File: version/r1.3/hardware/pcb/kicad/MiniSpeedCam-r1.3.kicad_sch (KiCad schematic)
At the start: 101 parts, among them J1 Power terminal connector, J10 TF PUSH, J3 Open Vias, J4 Open Vias, J8 AFC01-S24FCC-00, Q1 L8050QLT1G, Q2 L8050QLT1G, SW1 TS36CA-0.7, SW3 TS-1088-AR02016, SW6 TS-1088-AR02016, SW7 TS-1088-AR02016, SW8 TS-1088-AR02016, U12 MAX9814, U13 STM32F301K8Ux, U14 ESP32-S3-WROOM-1U-N8R8, U15 XC6206P282MR-G, U16 XC6206P122MR-G, U2 CH340X, U3 CH340X, U4 LMP7731MF, U5 B0505S-1W_C512032, U9 AP63203WU

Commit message: hardware(r1.3): add r1.3 PCB revision
Add the r1.3 KiCad design (MiniSpeedCam-r1.3.kicad_pcb/sch/pro/prl) with
refreshed footprint/symbol libraries and a freshly exported gerber set
(Gerber/ + Gerber.zip). Remove the stale 1.2-named fabrication outputs,
BOM, review image, README, and TO DO scratch file carried over from the
r1.2 seed.

Co-Authored-By: Claude Opus 4.8 <noreply@anthropic.com>
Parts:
- removed C1, C21, C25, C3: 1uF, Capacitor_SMD:C_0402_1005Metric, symbol 00-kiml-capacitors-smd:1u_0402_CL05A105KA5NQNC
- removed D4, D5, D6: SOD-523_BSD5C051L, Diode_SMD:D_SOD-523, symbol 00-kiml-power-protection:SOD-523_BSD5C051L
- removed Q1, Q2: L8050QLT1G, Package_TO_SOT_SMD:SOT-23, symbol Transistor_BJT:BC849
- removed R14, R15: 5.1K, Resistor_SMD:R_0402_1005Metric, symbol SparkFun-Resistor:5.1k_0402
- removed R20, R21: 10K, Resistor_SMD:R_0402_1005Metric, symbol SparkFun-Resistor:5.1k_0402
- removed R29: 1K, Resistor_SMD:R_0603_1608Metric, symbol Device:R
- removed SW6: TS-1088-AR02016, TS-1088-AR02016:SW-SMD_L3.9-W3.0-P4.45, symbol TS-1088-AR02016:TS-1088-AR02016
- removed U2, U3: CH340X, Package_SO:MSOP-10_3x3mm_P0.5mm, symbol Interface_USB:CH340E
- removed USB1: TYPE-C 16PIN 2MD(073), USB-C-LCSC_C2765186:USB-C-SMD_TYPE-C-6PIN-2MD-073, symbol C2765186:TYPE-C16PIN2MD(073)
- added R6: 10K, Resistor_SMD:R_0402_1005Metric, symbol SparkFun-Resistor:10k_0402
- C23, C53, C54, C56, C57: value 1uF -> 10u_0402_CL05A105KA5NQNC
- C48: value 22pF -> 22p_0402_0402CG220J500NT
- J1: value Power terminal connector -> 1984617
- J3: value Open Vias -> Conn_01x03_Female
- J4: value Open Vias -> Conn_01x06_Pin
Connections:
- net UART0_RXD_ESP32 is gone; now on net GPIO44: U14.36 (RXD0)
- net UART0_TXD_ESP32 is gone; now on net GPIO43: U14.37 (TXD0)
- net BOOT0: now also U14.22 (IO14), R6.1
- net CAM.RST: now also U14.15 (IO3); no longer U14.13 (IO19)
- net ESP_USB_D+: now also U14.14 (IO20)
- net ESP_USB_D-: now also U14.13 (IO19)
- net GND: now also R6.2
- net GPIO14: no longer U14.22 (IO14)
- net GPIO20 renamed GPIO43
- net GPIO43: no longer U14.14 (IO20)
- net GPIO3 renamed GPIO44
- net GPIO44: no longer U14.15 (IO3)
- no-connect marks 29 -> 27
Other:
- note removed: "CH340X is used with the ESP32 because a direct connection between the USB and native ESP32 USB results in unwanted behavior during sleep. When the ESP32 is placed into sleep mode, it disconnects the USB component, which makes debugging incredibly frustrating."
- note removed: "USB OTG"
- moved on the sheet: C19, C4, D7, J10, J4, R10, R16, R17, R18, R3, SW1, SW8

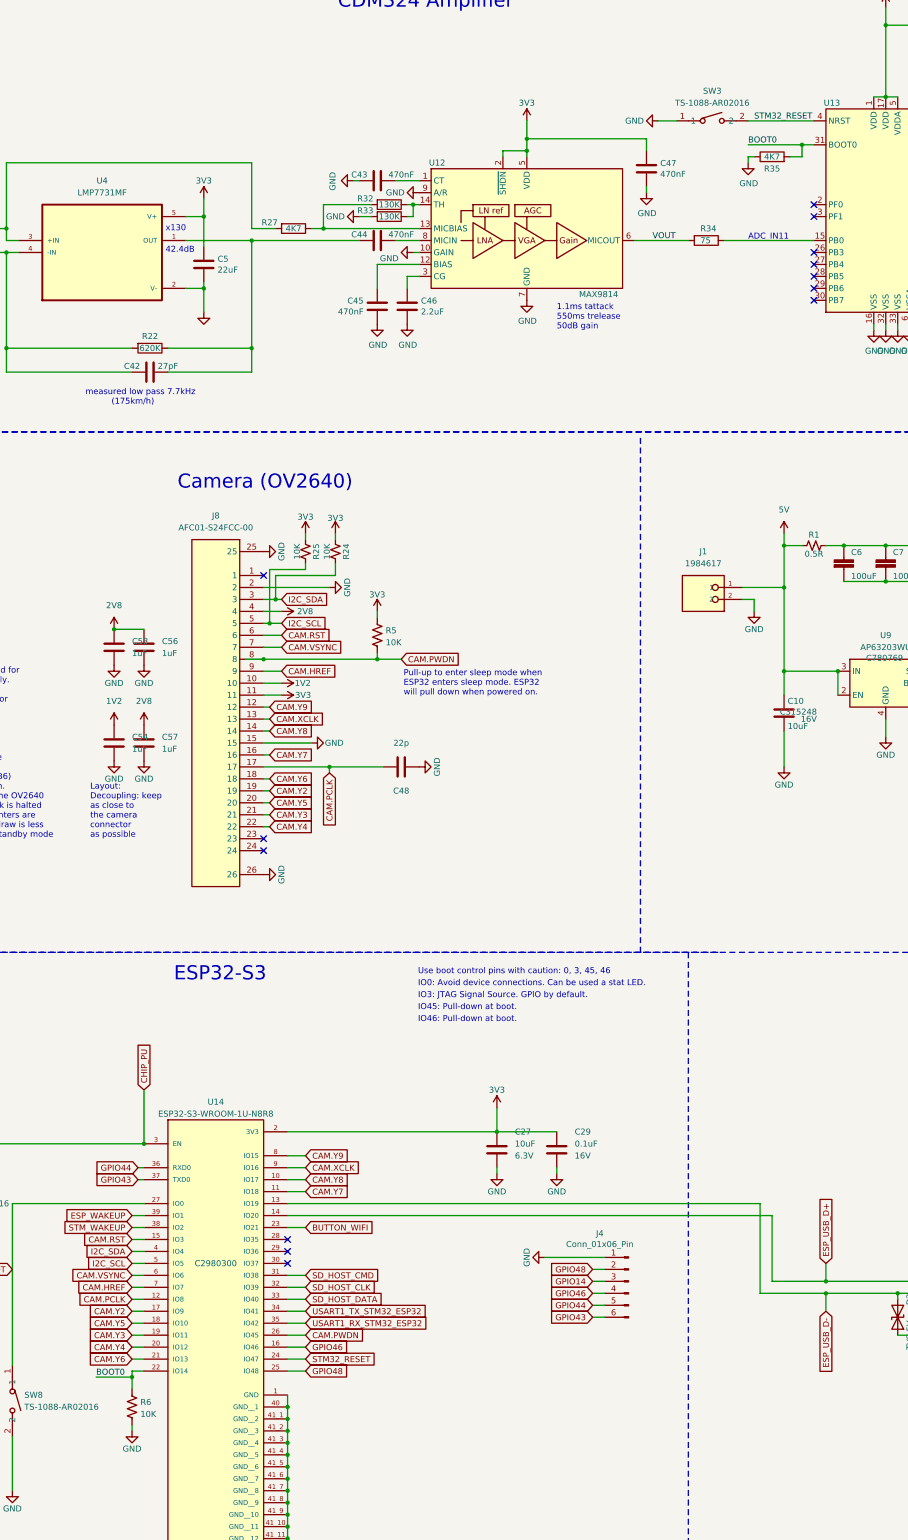
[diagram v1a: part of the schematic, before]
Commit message: hardware(r1.3): clean up r1.3 design files
Remove the stale gerber export set (Gerber/ and Gerber.zip, which were
plotted with the wrong 'lightspeed_r1' project name) and update the
board, schematic, and project-local settings.

Co-Authored-By: Claude Opus 4.8 <noreply@anthropic.com>
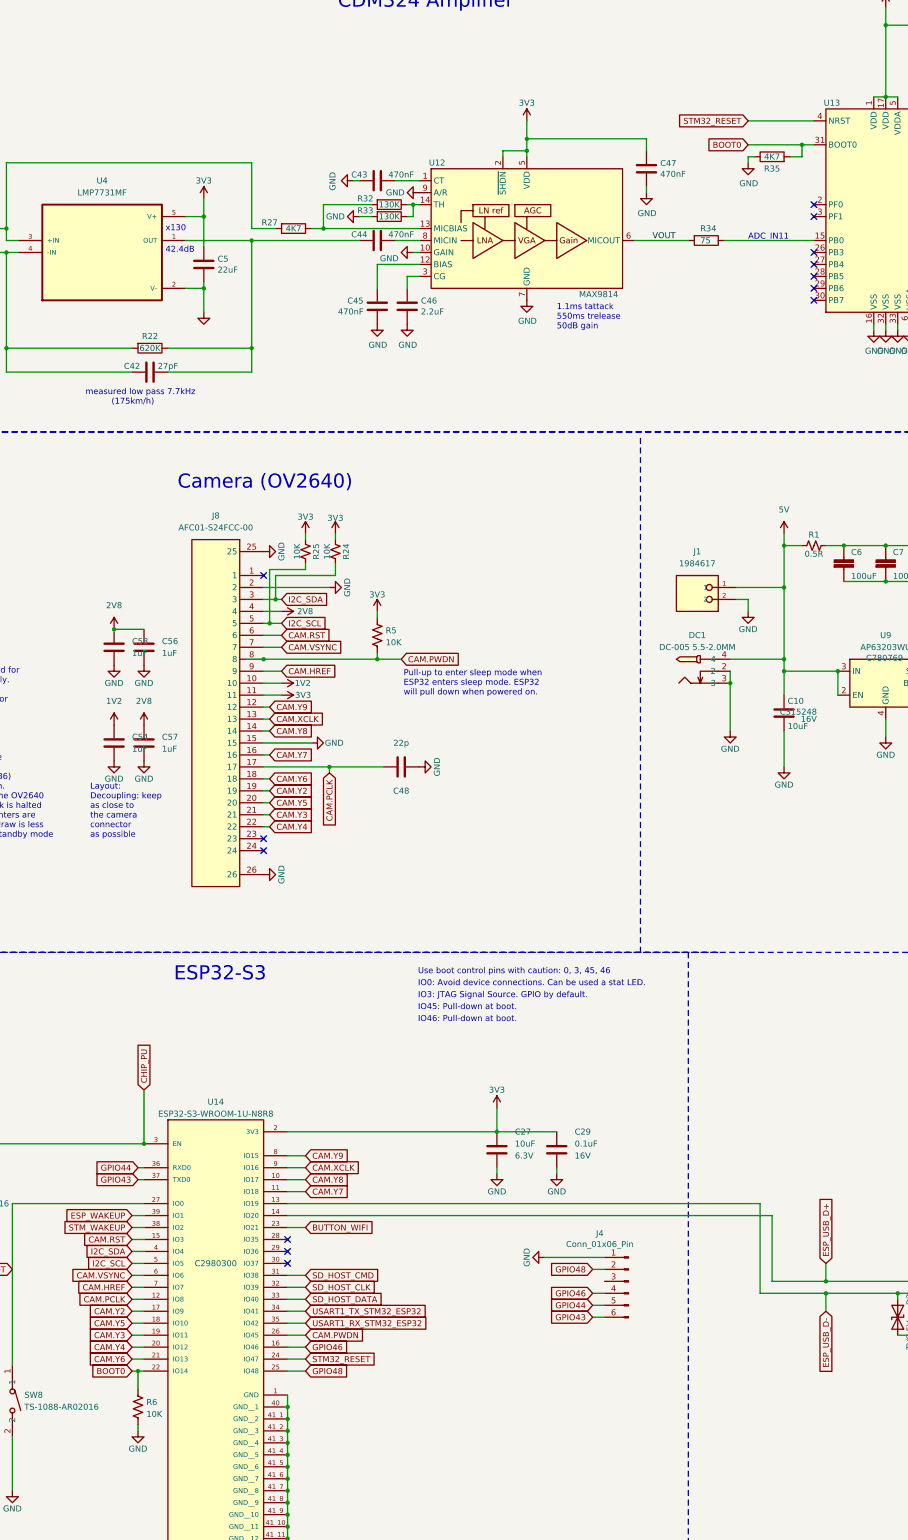
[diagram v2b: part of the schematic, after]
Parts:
- removed SW3: TS-1088-AR02016, TS-1088-AR02016:SW-SMD_L3.9-W3.0-P4.45, symbol TS-1088-AR02016:TS-1088-AR02016
- added DC1: DC-005 5.5-2.0MM, DC-005:DC-IN-TH_DC-005-5.5-2.0, symbol DC-005:DC-0055.5-2.0MM
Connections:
- net 5V: now also DC1.4
- net GND: now also DC1.2, DC1.3
- net GPIO14: no longer names the net of J4.3 (Pin_3)
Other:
- moved on the sheet: J1, R6
